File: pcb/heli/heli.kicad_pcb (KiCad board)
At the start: 4 copper layers, 50.6 x 50 mm, 68 parts, among them J1 Batterie, J2 Debug, J4 Servo, J5 Servo, M1 Motor_DC, M2 Motor_DC, Q1 IRLZ44N, Q2 BC547, Q3 IRLZ44N, Q4 BC547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

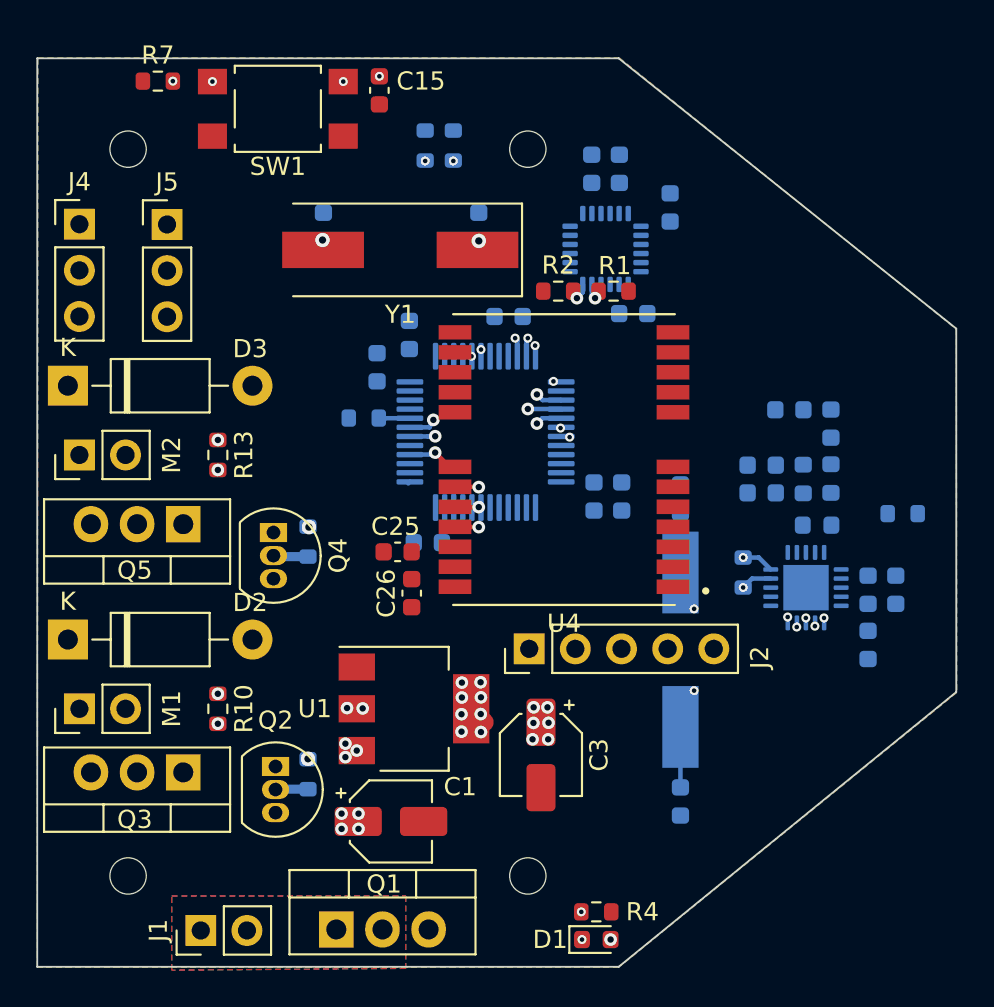
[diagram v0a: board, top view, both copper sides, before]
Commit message: 
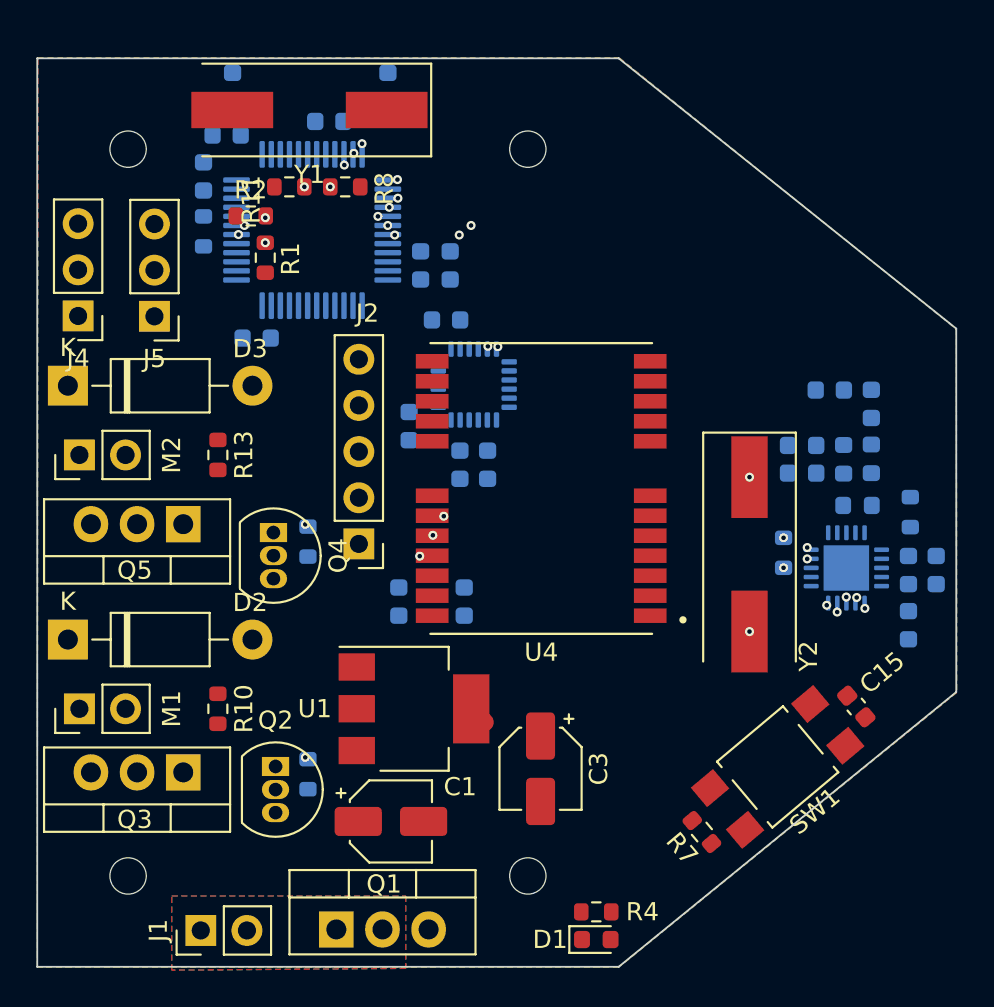
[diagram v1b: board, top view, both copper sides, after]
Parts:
- C25, C26: moved to B.Cu
- R11, R8, Y2: moved to F.Cu
- moved R7 51.0 mm to (54.6, 57.6), turned to 130 degrees
- moved SW1 45.5 mm to (58.8, 54.0), turned to 40 degrees
- moved C15 42.9 mm to (63.1, 50.7), turned to 130 degrees
- moved R1 19.3 mm to (30.6, 26.0), turned to 90 degrees
- moved C4 18.7 mm to (38.5, 35.2), turned to -90 degrees
- moved C5 18.5 mm to (41.3, 37.4), turned to -90 degrees
- moved R2 17.4 mm to (29.8, 23.7)
- moved C2 17.3 mm to (42.8, 37.4), turned to -90 degrees
- moved C12 15.9 mm to (39.1, 26.4)
- moved C14 15.8 mm to (40.7, 26.4)
- moved C13 14.9 mm to (28.4, 19.2), turned to 180 degrees
- moved C11 14.7 mm to (30.1, 30.4)
- moved U3 14.6 mm to (33.1, 24.4)
- moved C9 14.6 mm to (34.1, 18.5)
- moved C10 14.2 mm to (27.1, 21.5)
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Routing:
- net /PWM2: track 50.1 -> 22.5 mm
- net /PWM1: track 59.4 -> 33.5 mm
- net RADIO_CE: track 20.4 -> 45.1 mm, vias 2 -> 4
- net RADIO_CSN: track 19.4 -> 43.0 mm, vias 2 -> 4
- net SPI_MOSI: track 29.3 -> 44.6 mm
- net Net-(D3-Pad2): track 12.6 -> 0.00 mm
- net Net-(D2-Pad2): track 12.3 -> 0.00 mm
- net Net-(C6-Pad2): track 10.9 -> 0.00 mm, vias 2 -> 0
- net /SERVO1: track 26.9 -> 17.4 mm
- net Net-(C7-Pad2): track 9.83 -> 0.42 mm, vias 2 -> 0
- net SPI_MISO: track 33.7 -> 42.3 mm
- net SPI_SCK: track 35.1 -> 43.0 mm
- net Net-(C20-Pad1): track 13.5 -> 5.64 mm, vias 2 -> 3
- net Net-(Q4-Pad1): track 8.49 -> 1.46 mm, vias 1 -> 0
- net Net-(Q2-Pad1): track 7.58 -> 0.73 mm, vias 1 -> 0
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- added copper zone on In2.Cu, net 7.4V

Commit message: 
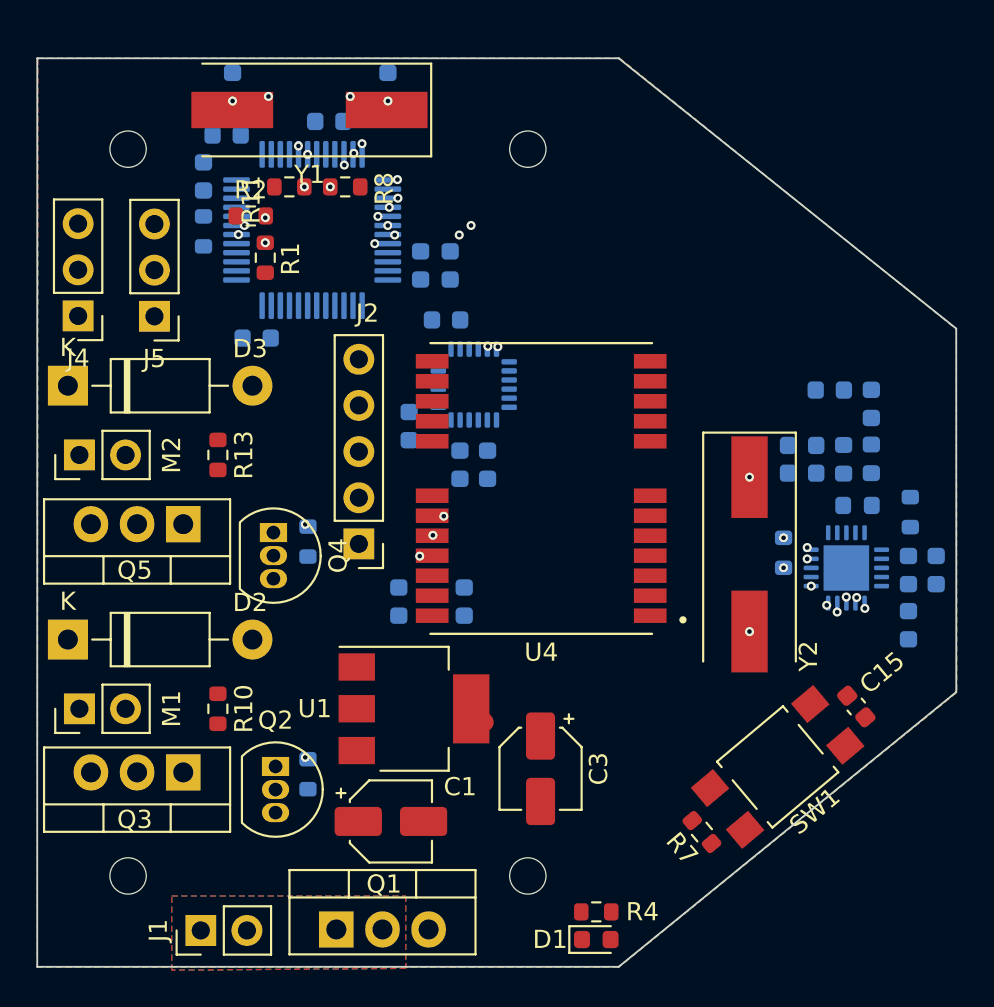
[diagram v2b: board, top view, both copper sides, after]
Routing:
- net RADIO_IRQ: track 0.00 -> 46.1 mm, vias 0 -> 4
- net Net-(C6-Pad2): track 0.00 -> 4.25 mm, vias 0 -> 3
- net Net-(C7-Pad2): track 0.42 -> 4.58 mm, vias 0 -> 3
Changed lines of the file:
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@@
   (via micro (at 35.875 19.7) (size 0.5) (drill 0.25) (layers "In1.Cu" "B.Cu") (net 1))
   (segment (start 41.885 50.8) (end 42.625 51.54) (width 1) (layer "F.Cu") (net 3))
+  (via micro (at 30.725 17.1) (size 0.5) (drill 0.25) (layers "F.Cu" "In2.Cu") (net 5))
+  (via (at 28.75 17.35) (size 0.5) (drill 0.25) (layers "F.Cu" "B.Cu") (net 5))
+  (segment (start 32.261392 18.07353) (end 32.261393 18.073529) (width 0.25) (layer "In2.Cu") (net 5))
+  (segment (start 31.732475 17.612499) (end 31.732474 17.6125) (width 0.25) (layer "In2.Cu") (net 5))
+  (segment (start 32.261394 17.578555) (end 32.261393 17.578555) (width 0.25) (layer "In2.Cu") (net 5))
+  (segment (start 32.261393 18.073529) (end 32.227449 18.107474) (width 0.25) (layer "In2.Cu") (net 5))
+  (segment (start 31.732474 17.6125) (end 31.766419 17.578556) (width 0.25) (layer "In2.Cu") (net 5))
+  (segment (start 30.725 17.1) (end 31.2375 17.6125) (width 0.25) (layer "In2.Cu") (net 5))
+  (segment (start 32.375 18.75) (end 32.375 19.825) (width 0.25) (layer "In2.Cu") (net 5))
+  (segment (start 32.227448 18.602448) (end 32.375 18.75) (width 0.25) (layer "In2.Cu") (net 5))
+  (segment (start 32.227448 18.602449) (end 32.227448 18.602448) (width 0.25) (layer "In2.Cu") (net 5))
+  (via micro (at 32.375 19.825) (size 0.5) (drill 0.25) (layers "In2.Cu" "B.Cu") (net 5))
+  (arc (start 32.261393 17.578555) (mid 32.363905 17.826043) (end 32.261392 18.07353) (width 0.25) (layer "In2.Cu") (net 5))
+  (arc (start 31.2375 17.6125) (mid 31.484988 17.715012) (end 31.732475 17.612499) (width 0.25) (layer "In2.Cu") (net 5))
+  (arc (start 32.227449 18.107474) (mid 32.124936 18.354961) (end 32.227448 18.602449) (width 0.25) (layer "In2.Cu") (net 5))
+  (arc (start 31.766419 17.578556) (mid 32.013906 17.476043) (end 32.261394 17.578555) (width 0.25) (layer "In2.Cu") (net 5))
+  (via micro (at 35.225 17.1) (size 0.5) (drill 0.25) (layers "F.Cu" "In2.Cu") (net 6))
+  (via (at 37.3 17.35) (size 0.5) (drill 0.25) (layers "F.Cu" "B.Cu") (net 6))
+  (segment (start 35.225 17.9425) (end 32.88 20.2875) (width 0.25) (layer "In2.Cu") (net 6))
+  (segment (start 35.225 17.1) (end 35.225 17.9425) (width 0.25) (layer "In2.Cu") (net 6))
+  (via micro (at 32.88 20.2875) (size 0.5) (drill 0.25) (layers "In2.Cu" "B.Cu") (net 6))
   (segment (start 37.3 17.35) (end 37 17.65) (width 0.25) (layer "B.Cu") (net 6))
   (segment (start 35.585 53.1) (end 35.665 53.18) (width 1) (layer "F.Cu") (net 10))
@@
   (segment (start 38.975 24.8) (end 38.975 40.45) (width 0.25) (layer "In2.Cu") (net 20))
   (via micro (at 37.375 23.2) (size 0.5) (drill 0.25) (layers "In2.Cu" "B.Cu") (net 20))
+  (segment (start 60.225 47.2) (end 60.575 47.2) (width 0.25) (layer "In1.Cu") (net 21))
+  (segment (start 40.1 45.65) (end 58.675 45.65) (width 0.25) (layer "In1.Cu") (net 21))
+  (segment (start 37.275 42.825) (end 40.1 45.65) (width 0.25) (layer "In1.Cu") (net 21))
+  (segment (start 58.675 45.65) (end 60.225 47.2) (width 0.25) (layer "In1.Cu") (net 21))
+  (via micro (at 37.275 42.825) (size 0.5) (drill 0.25) (layers "In1.Cu" "In2.Cu") (free) (net 21))
+  (via micro (at 60.575 47.2) (size 0.5) (drill 0.25) (layers "In1.Cu" "In2.Cu") (net 21))
+  (segment (start 36.925 42.475) (end 36.925 25.55) (width 0.25) (layer "In2.Cu") (net 21))
+  (segment (start 60.5935 47.1815) (end 60.575 47.2) (width 0.25) (layer "In2.Cu") (net 21))
+  (segment (start 60.5935 44.048) (end 60.5935 47.1815) (width 0.25) (layer "In2.Cu") (net 21))
+  (segment (start 36.925 25.55) (end 36.65 25.275) (width 0.25) (layer "In2.Cu") (net 21))
+  (segment (start 37.275 42.825) (end 36.925 42.475) (width 0.25) (layer "In2.Cu") (net 21))
+  (via micro (at 36.575 25.2) (size 0.5) (drill 0.25) (layers "In2.Cu" "B.Cu") (free) (net 21))
+  (via micro (at 60.5935 44.048) (size 0.5) (drill 0.25) (layers "In2.Cu" "B.Cu") (net 21))
   (segment (start 37.825 19.5) (end 36.725 18.4) (width 0.25) (layer "In1.Cu") (net 22))
   (segment (start 37.825 19.975) (end 37.825 19.5) (width 0.25) (layer "In1.Cu") (net 22))

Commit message: 
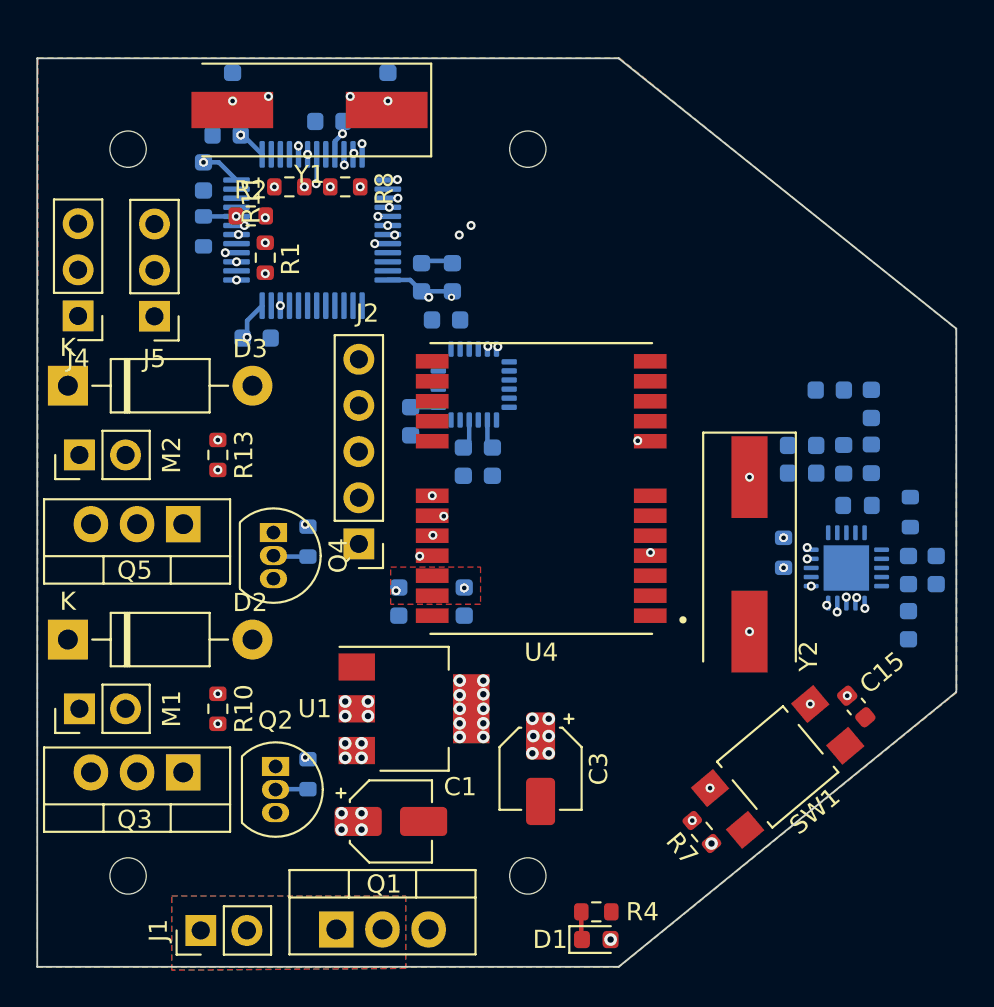
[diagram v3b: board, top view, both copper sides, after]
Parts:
- moved C14 0.66 mm to (40.9, 27.1)
- moved C12 0.65 mm to (39.1, 27.1)
- moved C2 0.31 mm to (43.0, 37.2)
- moved C4 0.28 mm to (38.5, 35.0)
- moved C5 0.25 mm to (41.5, 37.2)
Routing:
- net RESET: track 0.00 -> 65.1 mm, vias 0 -> 7
- net GPS_IRQ: track 0.00 -> 33.5 mm, vias 0 -> 5
- net GPS_CSN: track 0.00 -> 21.8 mm, vias 0 -> 3
- net SWCLK: track 0.00 -> 17.5 mm, vias 0 -> 1
- net 3.3V: track 1.05 -> 16.2 mm, vias 0 -> 34
- net Net-(D3-Pad2): track 0.00 -> 12.6 mm
- net Net-(D2-Pad2): track 0.00 -> 12.3 mm
- net SWDIO: track 0.00 -> 11.0 mm, vias 0 -> 1
- net Net-(Q2-Pad1): track 0.73 -> 9.41 mm, vias 0 -> 1
- net Net-(Q4-Pad1): track 1.46 -> 9.31 mm, vias 0 -> 1
- net Net-(Q4-Pad2): track 0.08 -> 1.92 mm
- net Net-(R5-Pad2): track 0.00 -> 1.82 mm
- net Net-(Q2-Pad2): track 0.03 -> 1.79 mm
- net GND: track 0.00 -> 1.66 mm
- net Net-(C5-Pad1): track 0.00 -> 1.65 mm
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- added copper zone on F.Cu, net 3.3V

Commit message: 
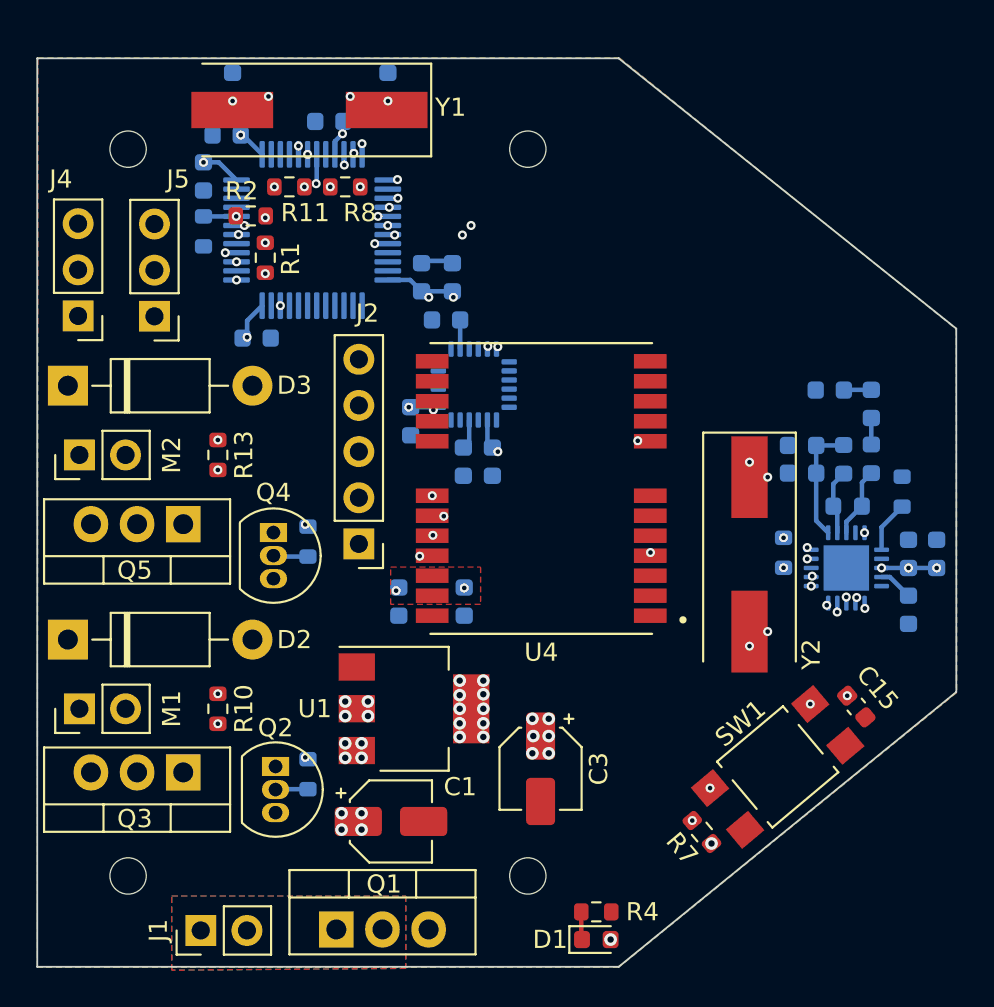
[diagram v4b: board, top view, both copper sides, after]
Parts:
- moved R3 1.21 mm to (65.6, 38.9)
- moved C23 0.89 mm to (67.5, 42.3), turned to 90 degrees
- moved C24 0.89 mm to (66.0, 42.3), turned to 90 degrees
- moved C16 0.85 mm to (66.0, 45.4)
- moved L1 0.54 mm to (62.6, 39.6)
- turned C17 to 90 degrees
- turned C20 to -90 degrees
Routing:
- net Net-(C18-Pad2): track 0.00 -> 6.60 mm
- net Net-(L1-Pad2): track 0.00 -> 3.85 mm
- net Net-(L1-Pad1): track 0.00 -> 3.58 mm
- net 3.3V: track 16.2 -> 19.1 mm, vias 34 -> 42
- net Net-(R3-Pad2): track 0.00 -> 2.84 mm
- net Net-(C16-Pad1): track 0.00 -> 1.91 mm
- net Net-(C8-Pad1): track 0.00 -> 1.61 mm
- net /Radio/50ohm: track 0.00 -> 1.52 mm
- net Net-(C21-Pad1): track 0.00 -> 1.46 mm
- net Net-(Q2-Pad1): track 9.41 -> 8.68 mm
- net Net-(C17-Pad1): track 5.97 -> 5.38 mm, vias 3 -> 4
- net Net-(C20-Pad1): track 5.64 -> 5.22 mm, vias 3 -> 4
